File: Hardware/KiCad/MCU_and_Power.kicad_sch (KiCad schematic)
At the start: 58 parts

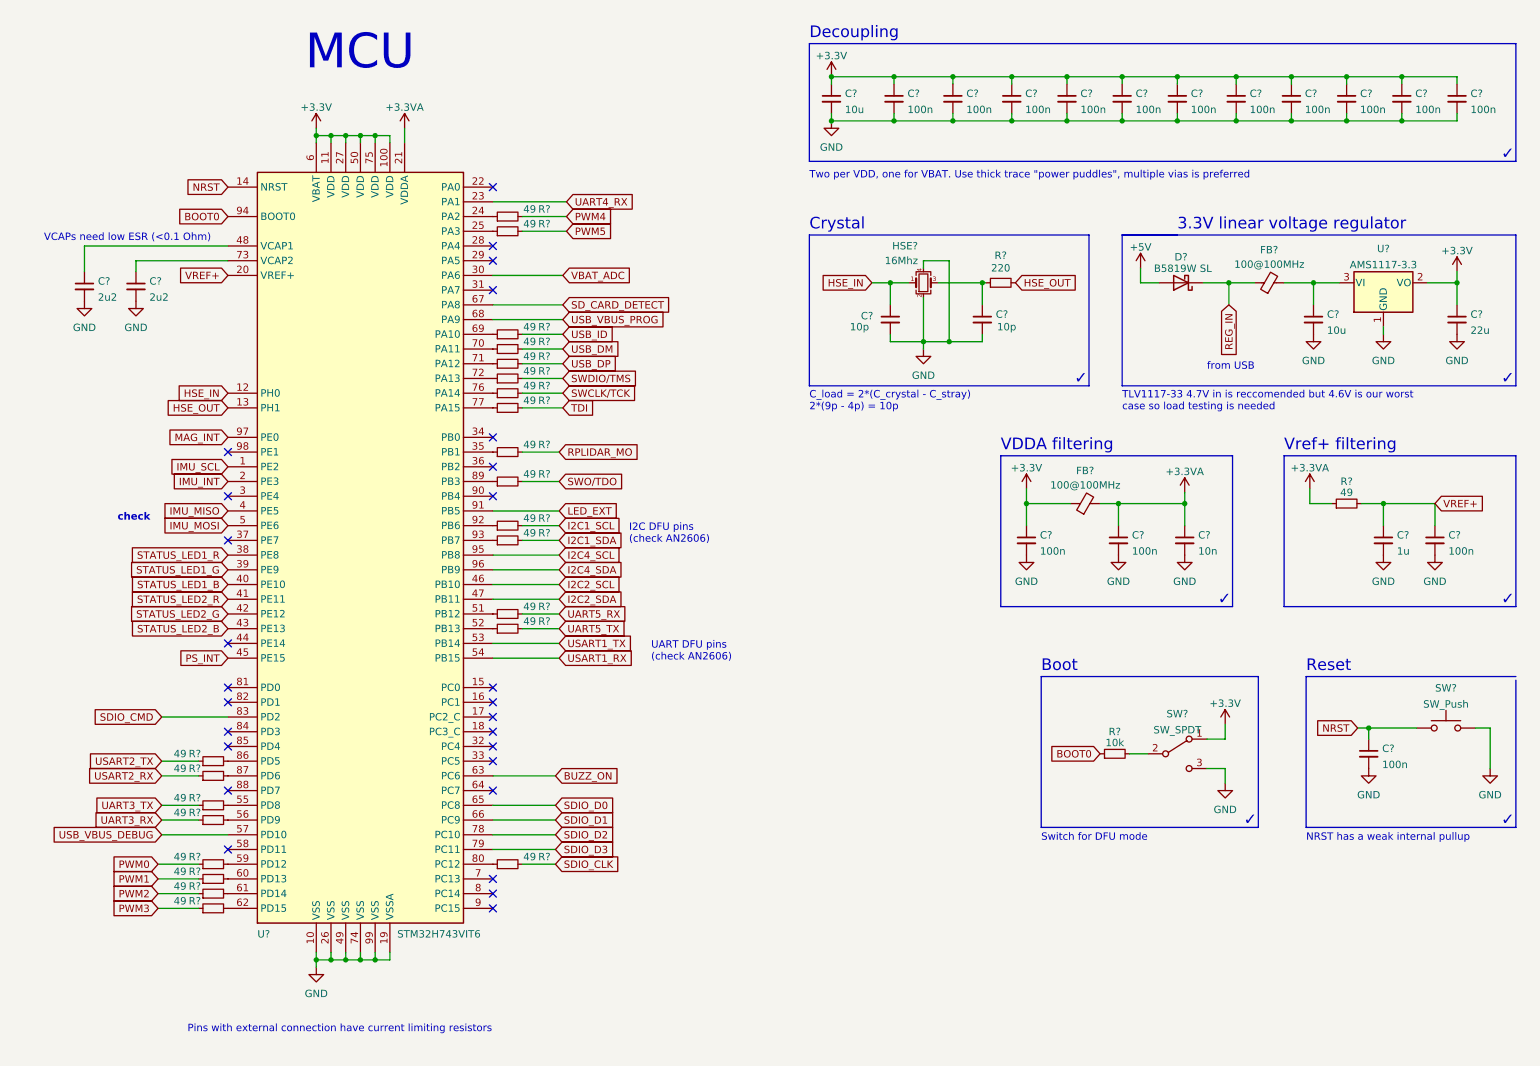
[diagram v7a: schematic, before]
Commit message: Added a footprint for an optional VBAT->5V regulator
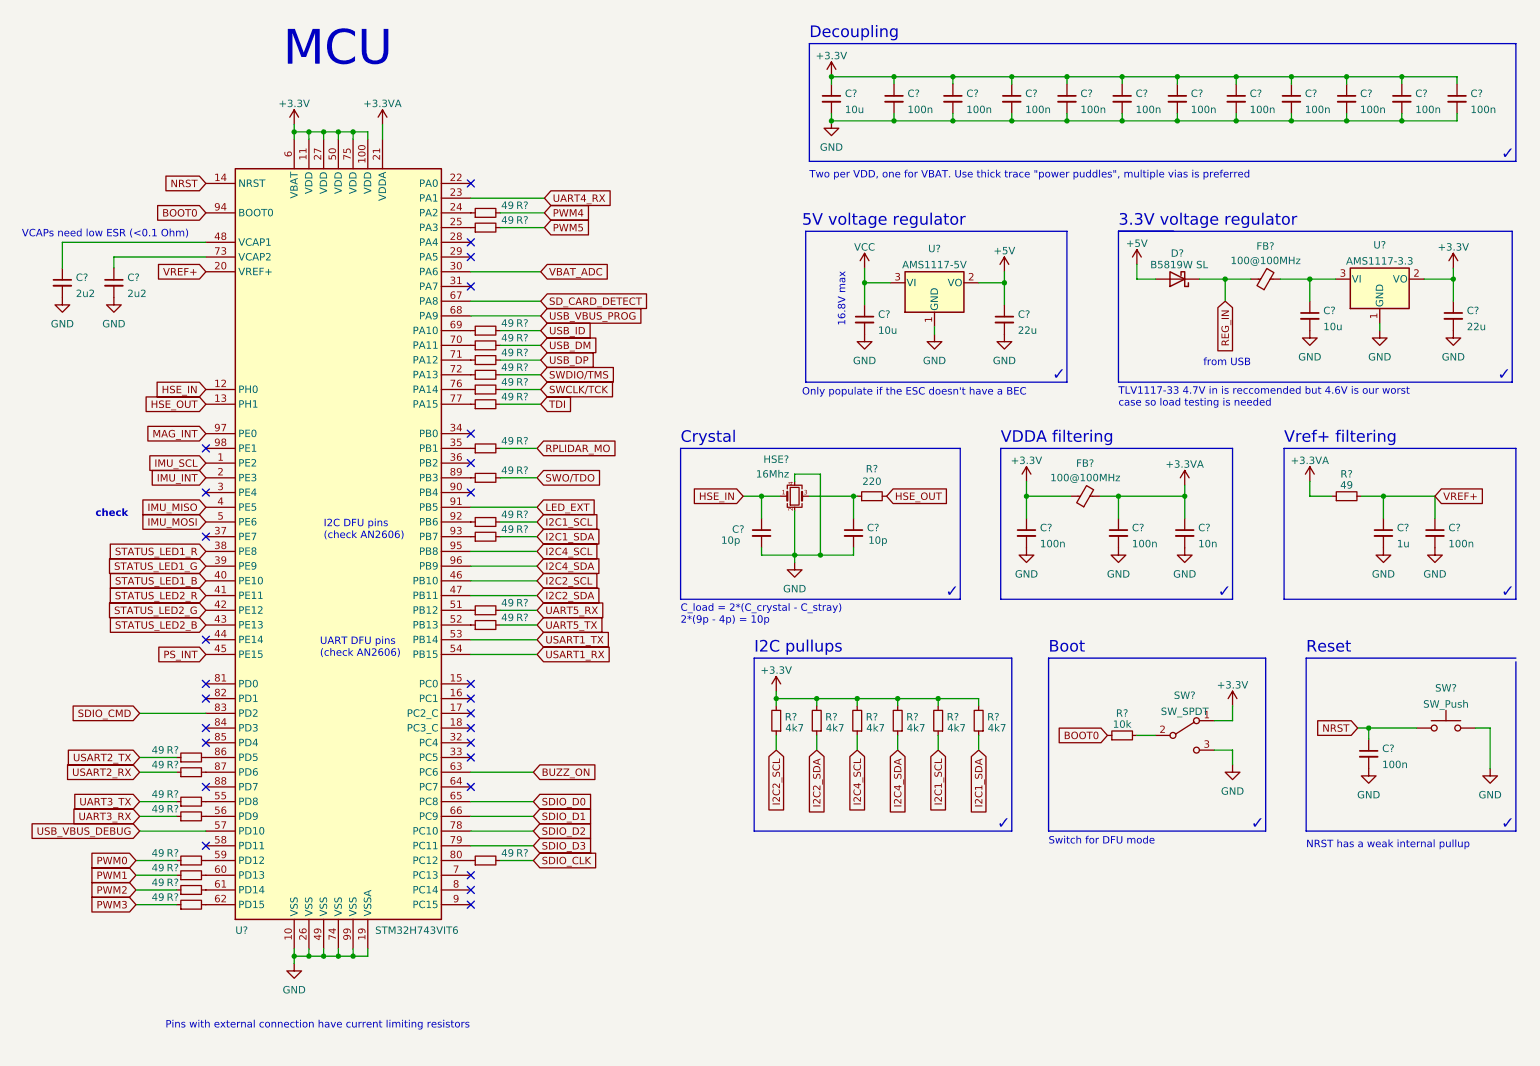
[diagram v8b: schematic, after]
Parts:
- added C?: 22u, Capacitor_SMD:C_0603_1608Metric, symbol Device:C_Small
- added C?: 10u, Capacitor_SMD:C_0603_1608Metric, symbol Device:C_Small
- added R? (x6): 4k7, Resistor_SMD:R_0402_1005Metric, symbol Device:R_Small
- added U?: AMS1117-5V, Package_TO_SOT_SMD:SOT-223-3_TabPin2, symbol Regulator_Linear:AMS1117-3.3
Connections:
- net +3V3: now also R?.2, R?.2, R?.2, R?.2, R?.2, R?.2
- net +5V: now also C?.1, U?.2 (VO)
- net GND: now also C?.2, C?.2, U?.1 (GND)
- net I2C1_SCL: now also R?.1
- net I2C1_SDA: now also R?.1
- net I2C2_SCL: now also R?.1
- net I2C2_SDA: now also R?.1
- net I2C4_SCL: now also R?.1
- net I2C4_SDA: now also R?.1
- new net VCC: C?.1, U?.3 (VI)
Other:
- note added: "16.8V max"
- note added: "3.3V voltage regulator"
- note added: "5V voltage regulator"
- note added: "I2C pullups"
- note added: "Only populate if the ESC doesn't have a BEC"
- note removed: "3.3V linear voltage regulator"
- moved on the sheet: C?, D?, FB?, HSE?, R?, SW?, U?
